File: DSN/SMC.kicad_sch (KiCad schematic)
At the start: 65 parts

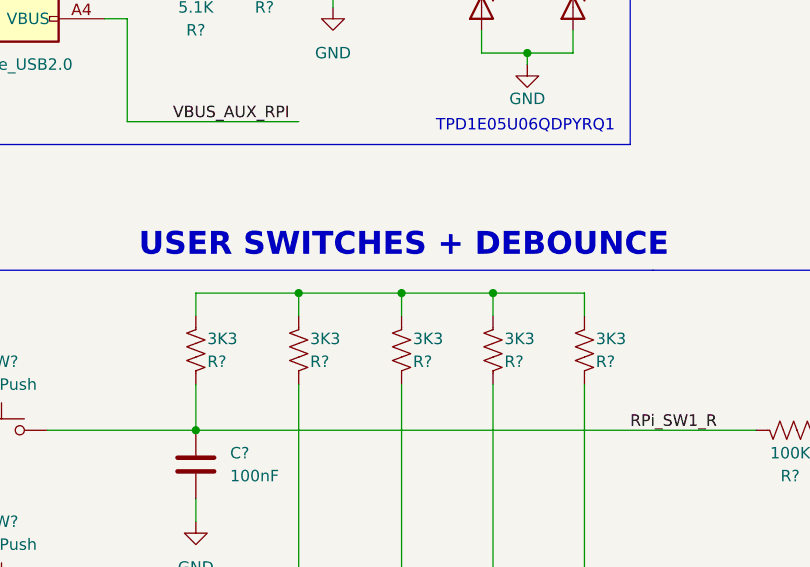
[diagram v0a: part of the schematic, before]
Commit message: Updates
Changed FPGA user io from 100 to 50 per chip, added 4 pmod per FPGA, added 8x buttons + led's, added SMA connectors for FPGA0 GTP.
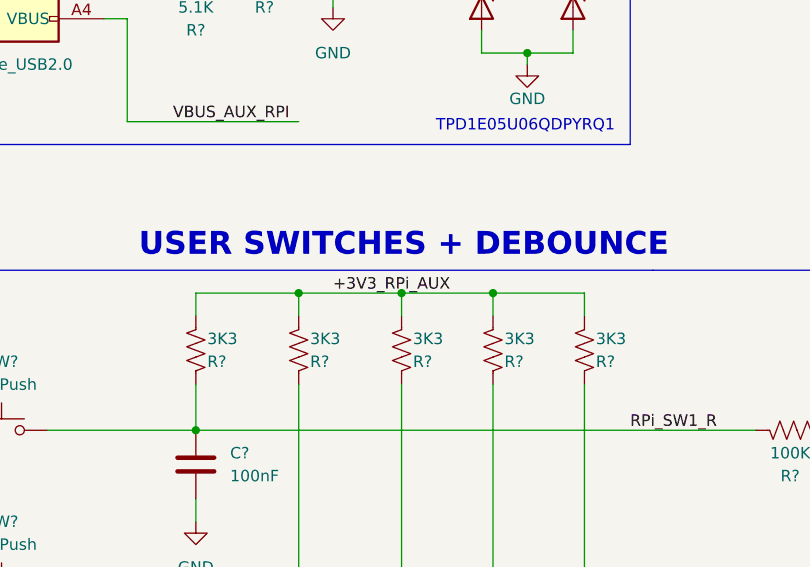
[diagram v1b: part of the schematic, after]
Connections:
- net +3V3_RPi_AUX: now also R?.1, R?.1, R?.1, R?.1, R?.1
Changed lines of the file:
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@@
+    (effects (font (size 1.27 1.27)) (justify left bottom))
+  )
+  (label "+3V3_RPi_AUX" (at 247.65 106.68 0)
     (effects (font (size 1.27 1.27)) (justify left bottom))
   )

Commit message: Added Footprints
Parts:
- removed R? (x2): 0R, Resistor_SMD:R_0402_1005Metric, symbol Device:R_US
- removed SW? (x4): SW_Push, symbol Switch:SW_Push
- added R? (x2): 0R, Resistor_SMD:R_0402_1005Metric, symbol Device:R_US
- added SW? (x4): SW_Push, Button_Switch_SMD:SW_SPST_B3SL-1022P, symbol Switch:SW_Push
- SW?: footprint (none) -> Button_Switch_SMD:SW_SPST_B3SL-1022P; MFR PN (none) -> B3SL-1022P
- U?: footprint (none) -> Package_SON:WSON-8-1EP_4x4mm_P0.8mm_EP2.2x3mm_ThermalVias; MFR PN (none) -> W25Q16JVUXIQ TR
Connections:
- net +3V3_RPi_AUX: now also R?.1, R?.2
- net DISP_3V3: now also R?.2
- net GND: now also SW?.1, SW?.1, SW?.1, SW?.1
- net RPi_SW2_R: now also SW?.2
- net RPi_SW3_R: now also SW?.2
- net RPi_SW4_R: now also SW?.2
- net RPi_SW5_R: now also SW?.2
- net SMC_3V3_AUX: now also R?.1

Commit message: Added component ref des
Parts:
- gave numbers to parts that had none: 65
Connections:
- net QSPI_SD2: now also U1.3 (WP_IO2)
- net SMC_TSNS_3: no longer names the net of U2.41 (GPIO29_ADC3)
- no-connect marks 5 -> 7

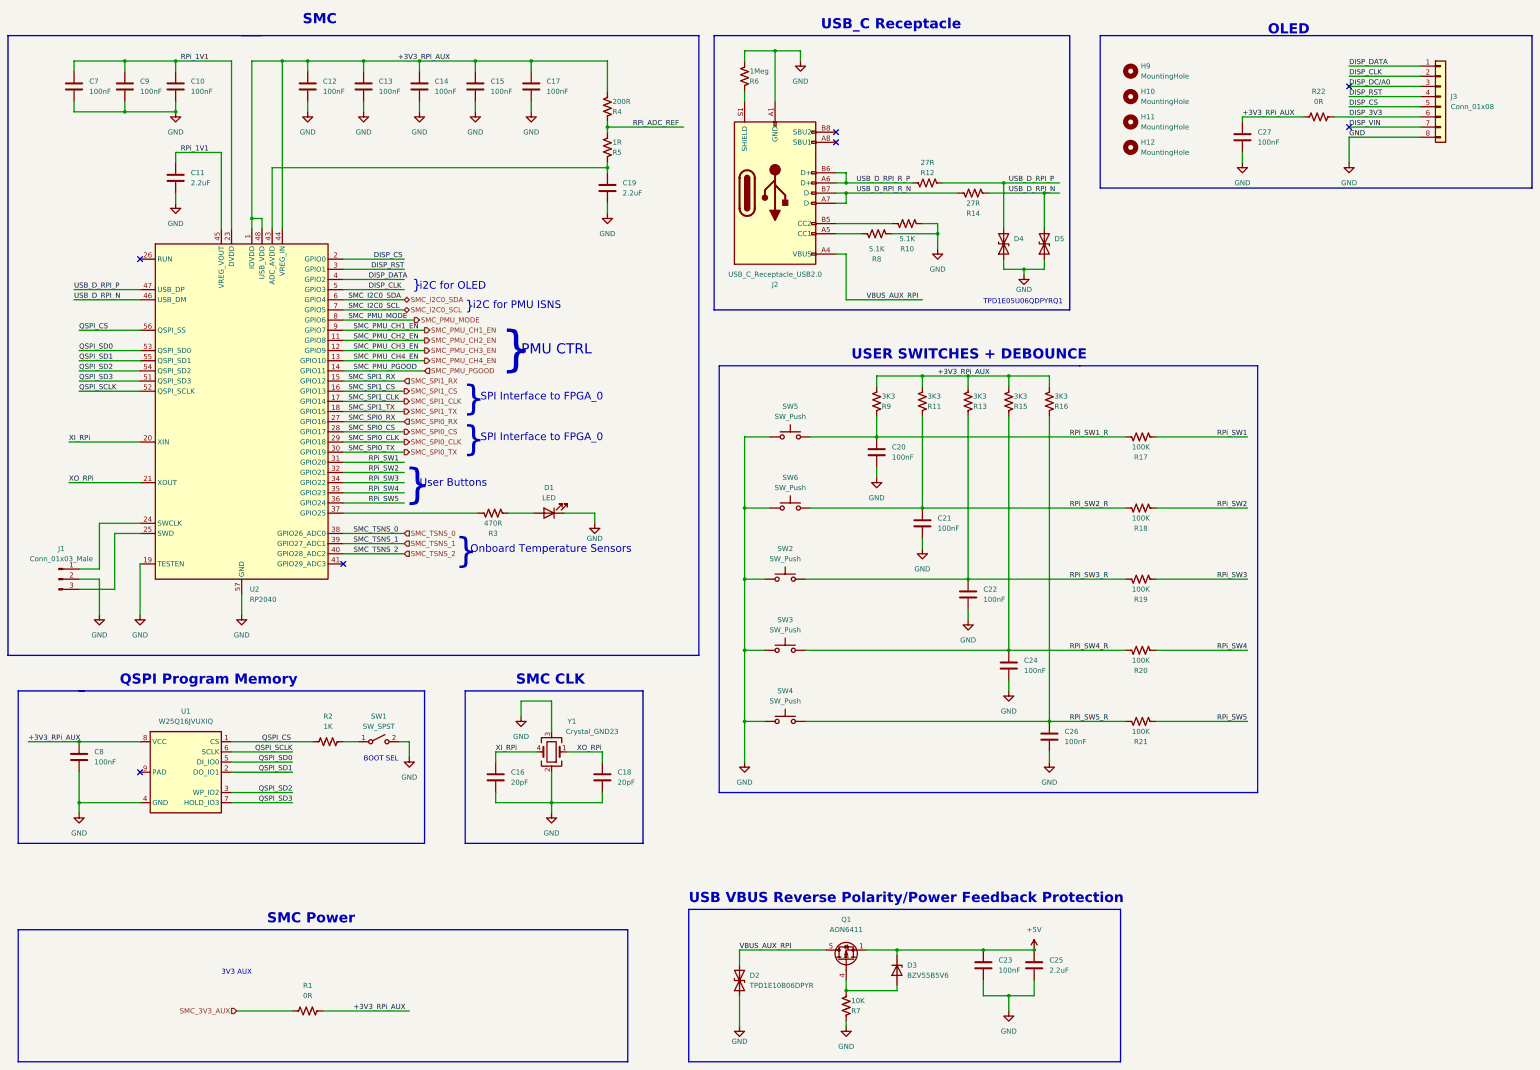
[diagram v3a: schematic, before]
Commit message: Fixed all ERC Errors
Warnings can be ignored
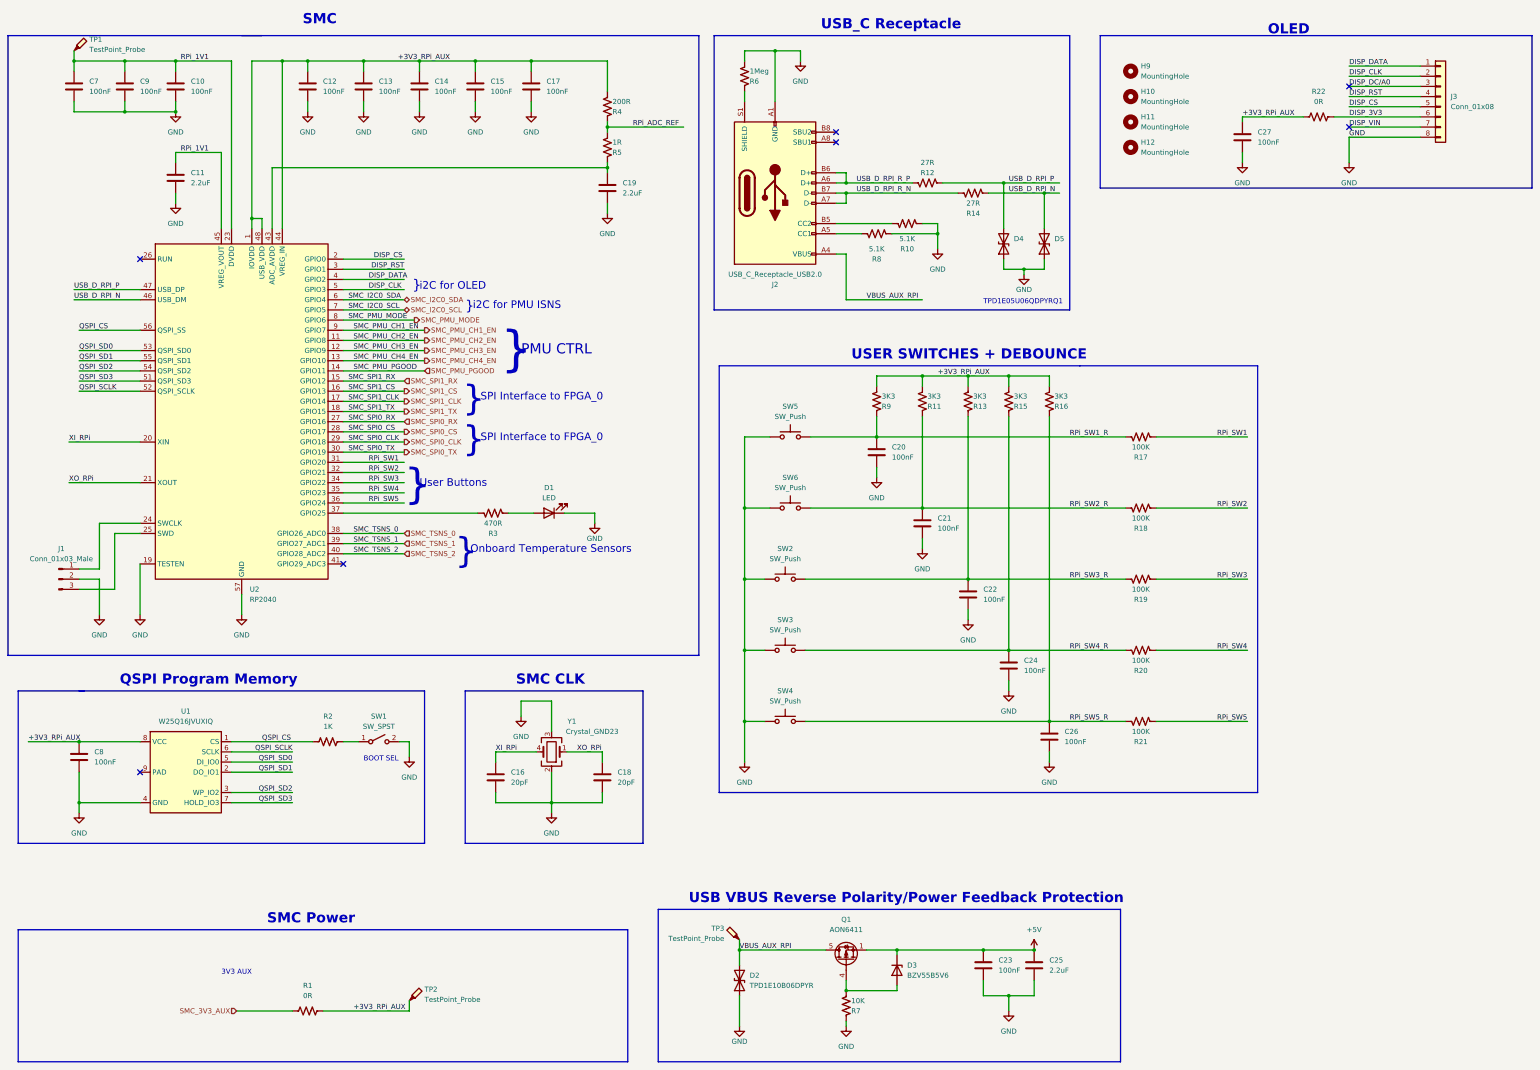
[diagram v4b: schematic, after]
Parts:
- added TP1, TP2, TP3: TestPoint_Probe, TestPoint:TestPoint_Loop_D2.50mm_Drill1.85mm, symbol Connector:TestPoint_Probe
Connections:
- net +3V3_RPi_AUX: now also TP2.1
- net RPi_1V1: now also TP1.1
- net VBUS_AUX_RPI: now also TP3.1
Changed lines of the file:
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@@
   (junction (at 243.84 106.68) (diameter 0) (color 0 0 0 0)
   )
+  (junction (at 198.12 250.19) (diameter 0) (color 0 0 0 0)
+  )
   (junction (at 165.1 44.45) (diameter 0) (color 0 0 0 0)
   )
@@
   )
   (junction (at 265.43 106.68) (diameter 0) (color 0 0 0 0)
+  )
+  (junction (at 31.75 27.94) (diameter 0) (color 0 0 0 0)
   )
   (junction (at 255.27 157.48) (diameter 0) (color 0 0 0 0)
@@
     (stroke (width 0) (type default) (color 0 0 0 0))
   )
-  (polyline (pts (xy 185.42 240.03) (xy 185.42 278.13))
+  (polyline (pts (xy 177.8 240.03) (xy 177.8 278.13))
     (stroke (width 0) (type default) (color 0 0 0 0))
   )
@@
     (stroke (width 0) (type default) (color 0 0 0 0))
   )
-  (polyline (pts (xy 185.42 278.13) (xy 293.37 278.13))
+  (polyline (pts (xy 177.8 278.13) (xy 293.37 278.13))
     (stroke (width 0) (type default) (color 0 0 0 0))
   )
@@
     (stroke (width 0) (type default) (color 0 0 0 0))
   )
+  (wire (pts (xy 31.75 25.4) (xy 31.75 27.94))
+    (stroke (width 0) (type default) (color 0 0 0 0))
+  )
   (wire (pts (xy 33.02 160.02) (xy 41.91 160.02))
     (stroke (width 0) (type default) (color 0 0 0 0))
@@
     (stroke (width 0) (type default) (color 0 0 0 0))
   )
-  (polyline (pts (xy 195.58 240.03) (xy 185.42 240.03))
+  (polyline (pts (xy 195.58 240.03) (xy 177.8 240.03))
     (stroke (width 0) (type default) (color 0 0 0 0))
   )
@@
     (stroke (width 0) (type default) (color 0 0 0 0))
   )
+  (wire (pts (xy 115.57 262.89) (xy 115.57 265.43))
+    (stroke (width 0) (type default) (color 0 0 0 0))
+  )
   (wire (pts (xy 151.13 187.96) (xy 143.51 187.96))
     (stroke (width 0) (type default) (color 0 0 0 0))
@@
   )
   (wire (pts (xy 33.02 107.95) (xy 48.26 107.95))
+    (stroke (width 0) (type default) (color 0 0 0 0))
+  )
+  (wire (pts (xy 198.12 247.65) (xy 198.12 250.19))
     (stroke (width 0) (type default) (color 0 0 0 0))
   )
@@
     (pin "2")
   )
+  (symbol (lib_id "Connector:TestPoint_Probe") (at 198.12 247.65 0) (mirror y) (unit 1)
+    (in_bom yes) (on_board yes)
+    (property "Reference" "TP3" (id 0) (at 194.31 244.7924 0)
+      (effects (font (size 1.27 1.27)) (justify left))
+    )
+    (property "Value" "TestPoint_Probe" (id 1) (at 194.31 247.3324 0)
+      (effects (font (size 1.27 1.27)) (justify left))
+    )
+    (property "Footprint" "TestPoint:TestPoint_Loop_D2.50mm_Drill1.85mm" (id 2) (at 193.04 247.65 0)
+      (effects (font (size 1.27 1.27)) hide)
+    )
+    (property "Datasheet" "~" (id 3) (at 193.04 247.65 0)
+      (effects (font (size 1.27 1.27)) hide)
+    )
+    (pin "1")
+  )
   (symbol (lib_id "power:GND") (at 323.85 53.34 0) (unit 1)
     (in_bom yes) (on_board yes) (fields_autoplaced)
@@
     )
     (property "Datasheet" "" (id 3) (at 265.43 185.42 0)
+      (effects (font (size 1.27 1.27)) hide)
+    )
+    (pin "1")
+  )
+  (symbol (lib_id "Connector:TestPoint_Probe") (at 115.57 262.89 0) (unit 1)
+    (in_bom yes) (on_board yes)
+    (property "Reference" "TP2" (id 0) (at 119.38 260.0324 0)
+      (effects (font (size 1.27 1.27)) (justify left))
+    )
+    (property "Value" "TestPoint_Probe" (id 1) (at 119.38 262.5724 0)
+      (effects (font (size 1.27 1.27)) (justify left))
+    )
+    (property "Footprint" "TestPoint:TestPoint_Loop_D2.50mm_Drill1.85mm" (id 2) (at 120.65 262.89 0)
+      (effects (font (size 1.27 1.27)) hide)
+    )
+    (property "Datasheet" "~" (id 3) (at 120.65 262.89 0)
       (effects (font (size 1.27 1.27)) hide)
     )
@@
     (pin "2")
   )
+  (symbol (lib_id "Connector:TestPoint_Probe") (at 31.75 25.4 0) (unit 1)
+    (in_bom yes) (on_board yes)
+    (property "Reference" "TP1" (id 0) (at 35.56 22.5424 0)
+      (effects (font (size 1.27 1.27)) (justify left))
+    )
+    (property "Value" "TestPoint_Probe" (id 1) (at 35.56 25.0824 0)
+      (effects (font (size 1.27 1.27)) (justify left))
+    )
+    (property "Footprint" "TestPoint:TestPoint_Loop_D2.50mm_Drill1.85mm" (id 2) (at 36.83 25.4 0)
+      (effects (font (size 1.27 1.27)) hide)
+    )
+    (property "Datasheet" "~" (id 3) (at 36.83 25.4 0)
+      (effects (font (size 1.27 1.27)) hide)
+    )
+    (pin "1")
+  )
   (symbol (lib_id "power:GND") (at 224.79 269.24 0) (unit 1)

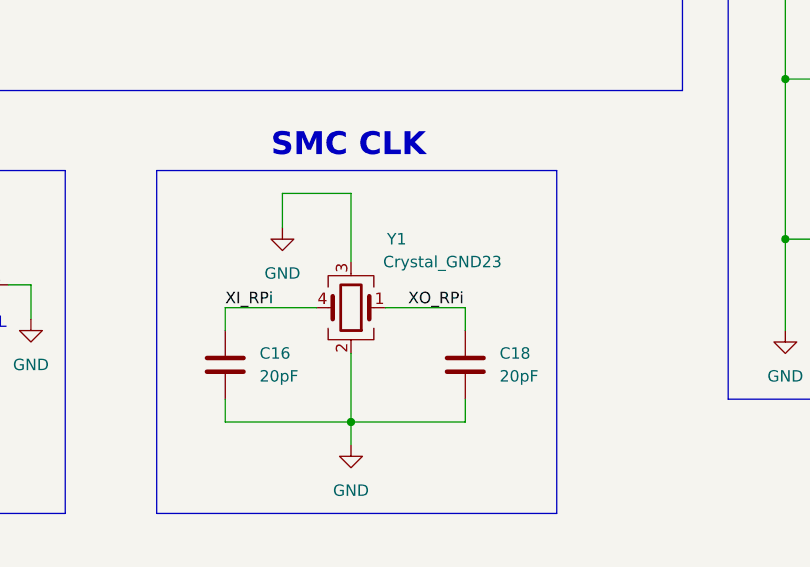
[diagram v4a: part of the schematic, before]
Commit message: Initial PCB Layout
Initial layout and part placement
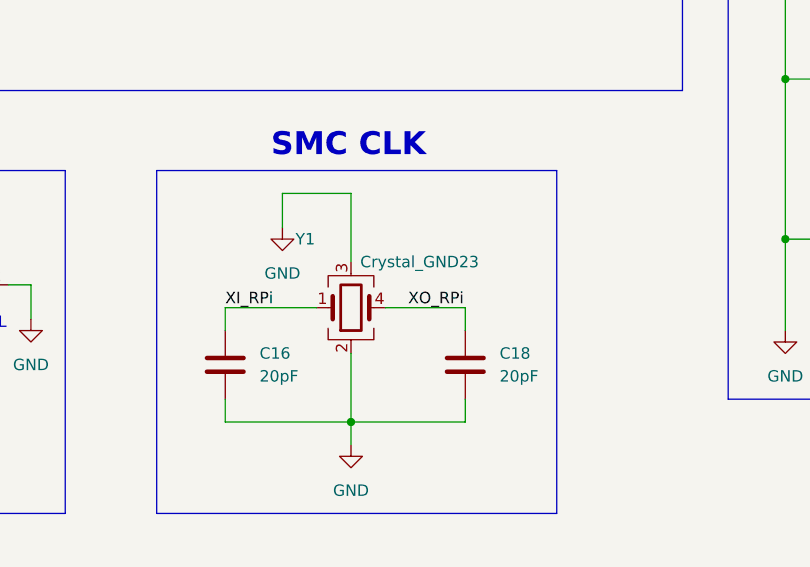
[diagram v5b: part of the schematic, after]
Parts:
- J1: footprint (none) -> Connector_PinHeader_2.54mm:PinHeader_1x03_P2.54mm_Vertical
- J3: footprint (none) -> Connector_PinHeader_2.54mm:PinHeader_1x08_P2.54mm_Vertical
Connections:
- net XI_RPi: now also Y1.1; no longer Y1.4
- net XO_RPi: now also Y1.4; no longer Y1.1
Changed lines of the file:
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@@
     (pin "1")
+  )
+  (symbol (lib_id "Device:Crystal_GND23") (at 151.13 200.66 0) (mirror x) (unit 1)
+    (in_bom yes) (on_board yes)
+    (property "Reference" "Y1" (id 0) (at 146.05 193.04 0))
+    (property "Value" "Crystal_GND23" (id 1) (at 158.75 195.58 0))
+    (property "Footprint" "Crystal:Crystal_SMD_3225-4Pin_3.2x2.5mm" (id 2) (at 151.13 200.66 0)
+      (effects (font (size 1.27 1.27)) hide)
+    )
+    (property "Datasheet" "~" (id 3) (at 151.13 200.66 0)
+      (effects (font (size 1.27 1.27)) hide)
+    )
+    (property "MFR PN" "12M20P2/XT324-10/10" (id 4) (at 151.13 200.66 90)
+      (effects (font (size 1.27 1.27)) hide)
+    )
+    (pin "1")
+    (pin "2")
+    (pin "3")
+    (pin "4")
   )
   (symbol (lib_id "power:GND") (at 33.02 215.9 0) (unit 1)
@@
       (effects (font (size 1.27 1.27)) (justify left))
     )
-    (property "Footprint" "" (id 2) (at 373.38 36.83 0)
+    (property "Footprint" "Connector_PinHeader_2.54mm:PinHeader_1x08_P2.54mm_Vertical" (id 2) (at 373.38 36.83 0)
       (effects (font (size 1.27 1.27)) hide)
     )
@@
     (property "Reference" "J1" (id 0) (at 28.575 149.86 0))
     (property "Value" "Conn_01x03_Male" (id 1) (at 28.575 152.4 0))
-    (property "Footprint" "" (id 2) (at 27.94 157.48 0)
+    (property "Footprint" "Connector_PinHeader_2.54mm:PinHeader_1x03_P2.54mm_Vertical" (id 2) (at 27.94 157.48 0)
       (effects (font (size 1.27 1.27)) hide)
     )
@@
     (pin "1")
   )
-  (symbol (lib_id "Device:Crystal_GND23") (at 151.13 200.66 180) (unit 1)
-    (in_bom yes) (on_board yes)
-    (property "Reference" "Y1" (id 0) (at 156.21 193.04 0))
-    (property "Value" "Crystal_GND23" (id 1) (at 161.29 195.58 0))
-    (property "Footprint" "Crystal:Crystal_SMD_3225-4Pin_3.2x2.5mm" (id 2) (at 151.13 200.66 0)
-      (effects (font (size 1.27 1.27)) hide)
-    )
-    (property "Datasheet" "~" (id 3) (at 151.13 200.66 0)
-      (effects (font (size 1.27 1.27)) hide)
-    )
-    (property "MFR PN" "12M20P2/XT324-10/10" (id 4) (at 151.13 200.66 90)
-      (effects (font (size 1.27 1.27)) hide)
-    )
-    (pin "1")
-    (pin "2")
-    (pin "3")
-    (pin "4")
-  )
   (symbol (lib_id "MCU_RaspberryPi:RP2040") (at 73.66 115.57 0) (unit 1)

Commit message: Updated Layout
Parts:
- removed C21, C22, C24, C26: 100nF, Capacitor_SMD:C_0402_1005Metric, symbol Device:C
- removed D3: BZV55B5V6, Diode_SMD:D_MiniMELF, symbol Diode:BZV55B5V6
- removed H11, H12: MountingHole, MountingHole:MountingHole_3.5mm, symbol Mechanical:MountingHole
- removed R11, R13, R15, R16: 3K3, Resistor_SMD:R_0402_1005Metric, symbol Device:R_US
- removed R18, R19, R20, R21: 100K, Resistor_SMD:R_0402_1005Metric, symbol Device:R_US
- removed SW2, SW3, SW4, SW6: SW_Push, Button_Switch_SMD:SW_SPST_B3SL-1022P, symbol Switch:SW_Push
- removed Y1: Crystal_GND23, Crystal:Crystal_SMD_3225-4Pin_3.2x2.5mm, symbol Device:Crystal_GND23
- added D3: 5.6V Zener, Diode_SMD:D_SOD-123, symbol Device:D_Zener
- added Y1: Crystal_GND24, Crystal:Crystal_SMD_3225-4Pin_3.2x2.5mm, symbol Device:Crystal_GND24
- TP1, TP2, TP3: footprint TestPoint:TestPoint_Loop_D2.50mm_Drill1.85mm -> TestPoint:TestPoint_Loop_D1.80mm_Drill1.0mm_Beaded
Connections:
- net +5V: now also D3.1 (K)
- net GND: now also Y1.2, Y1.4
- net XI_RPi: now also Y1.1
- net XO_RPi: now also Y1.3
- net at Q1.4 (G), R7.1: now also D3.2 (A)
- net RPi_SW2 renamed SMC_IO0
- net RPi_SW3 renamed SMC_IO1
- net RPi_SW4 renamed SMC_IO2
- net RPi_SW5 renamed SMC_IO3
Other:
- note added: "USER SWITCH + DEBOUNCE"
- note removed: "USER SWITCHES + DEBOUNCE"
- note removed: "User Buttons"
